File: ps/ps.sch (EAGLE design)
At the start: 66 parts, among them IC1 LM675, Q1 NPN-D, Q2 NPN-D, U1 LM3480IM4, U2 LM317, U3 TLC555CD, U4 LM317, U5 LM317

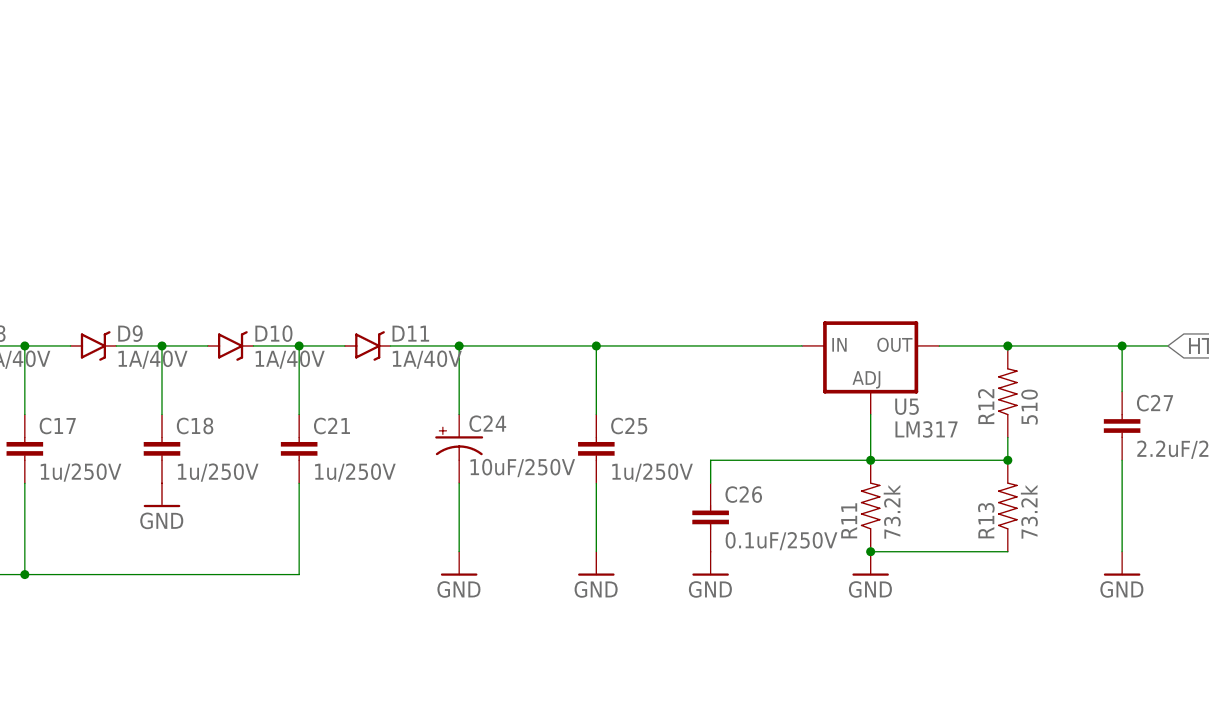
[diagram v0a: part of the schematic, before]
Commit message: Back to 60V supply
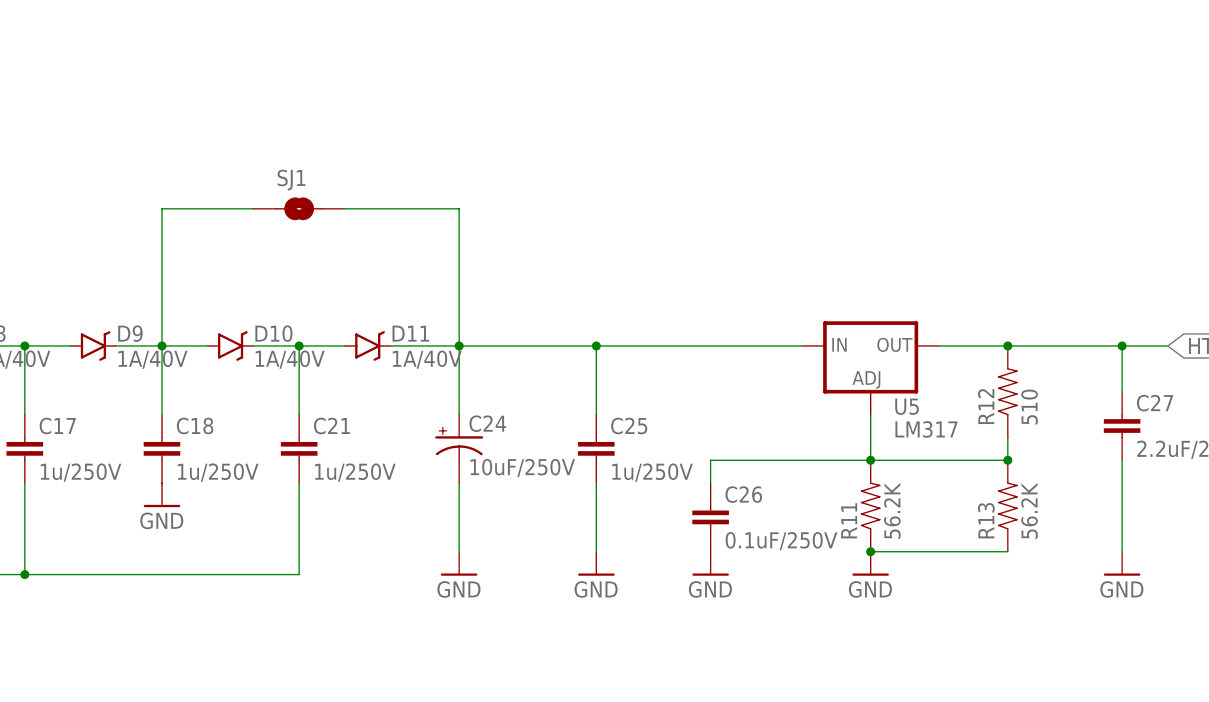
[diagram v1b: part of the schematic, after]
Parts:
- added SJ1: SOLDERJUMPERROUND, my:SOLDERJUMPERROUND
- R11, R13: value 73.2k -> 56.2K
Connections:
- net HV: now also SJ1.2
- net N$15: now also SJ1.1
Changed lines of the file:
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@@
 <part name="C25" library="rcl" deviceset="C-EU" device="C2220K" value="1u/250V"/>
 <part name="GND20" library="SparkFun-Aesthetics" deviceset="GND" device=""/>
-<part name="R11" library="SparkFun-Resistors" deviceset="RESISTOR" device="PTH-1/4W" value="73.2k"/>
-<part name="R13" library="SparkFun-Resistors" deviceset="RESISTOR" device="PTH-1/4W" value="73.2k"/>
+<part name="R11" library="SparkFun-Resistors" deviceset="RESISTOR" device="PTH-1/4W" value="56.2K"/>
+<part name="R13" library="SparkFun-Resistors" deviceset="RESISTOR" device="PTH-1/4W" value="56.2K"/>
 <part name="GND22" library="SparkFun-Aesthetics" deviceset="GND" device=""/>
 <part name="R12" library="SparkFun-Resistors" deviceset="RESISTOR" device="PTH-1/4W" value="510"/>
@@
 <part name="GND24" library="SparkFun-Aesthetics" deviceset="GND" device=""/>
 <part name="R14" library="SparkFun-Resistors" deviceset="100KOHM-1/10W-1%(0603)" device="" value="100k"/>
+<part name="SJ1" library="my" deviceset="SOLDERJUMPER" device="ROUND" value=""/>
 </parts>
 <sheets>
@@
 <instance part="GND24" gate="1" x="109.22" y="200.66" rot="R90"/>
 <instance part="R14" gate="G$1" x="119.38" y="203.2"/>
+<instance part="SJ1" gate="1" x="269.24" y="121.92"/>
 </instances>
 <busses>
@@
 <wire x1="254" y1="99.06" x2="254" y2="106.68" width="0.1524" layer="91"/>
 <junction x="254" y="106.68"/>
+<wire x1="254" y1="106.68" x2="254" y2="121.92" width="0.1524" layer="91"/>
+<pinref part="SJ1" gate="1" pin="1"/>
+<wire x1="254" y1="121.92" x2="264.16" y2="121.92" width="0.1524" layer="91"/>
 </segment>
 </net>
@@
 <wire x1="302.26" y1="99.06" x2="302.26" y2="106.68" width="0.1524" layer="91"/>
 <junction x="302.26" y="106.68"/>
-</segment>
-<segment>
+<pinref part="SJ1" gate="1" pin="2"/>
+<wire x1="274.32" y1="121.92" x2="287.02" y2="121.92" width="0.1524" layer="91"/>
+<wire x1="287.02" y1="121.92" x2="287.02" y2="106.68" width="0.1524" layer="91"/>
+</segment>
+<segment>

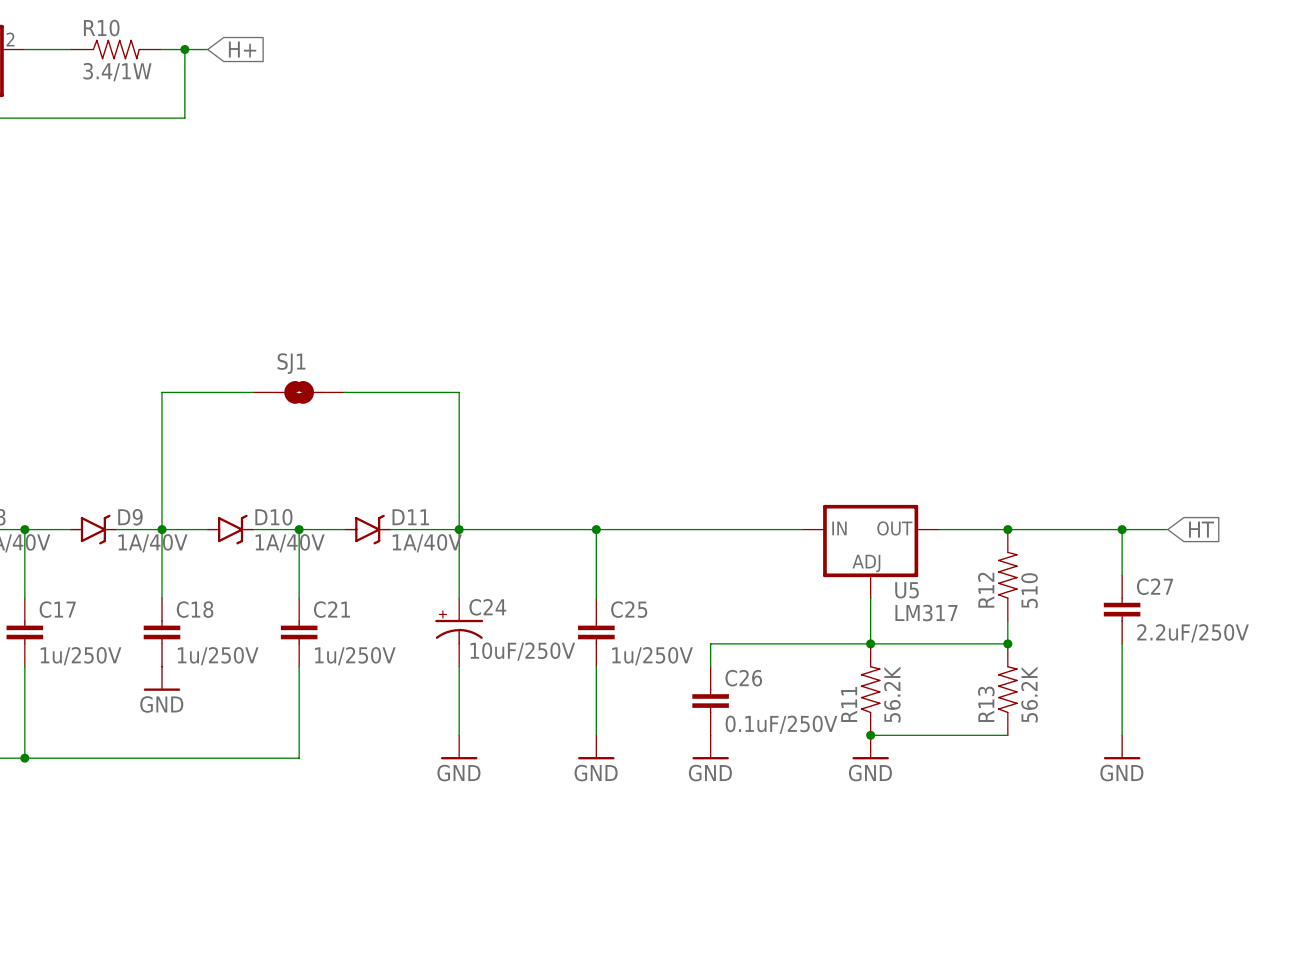
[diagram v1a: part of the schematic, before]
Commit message: HV for neon bulb
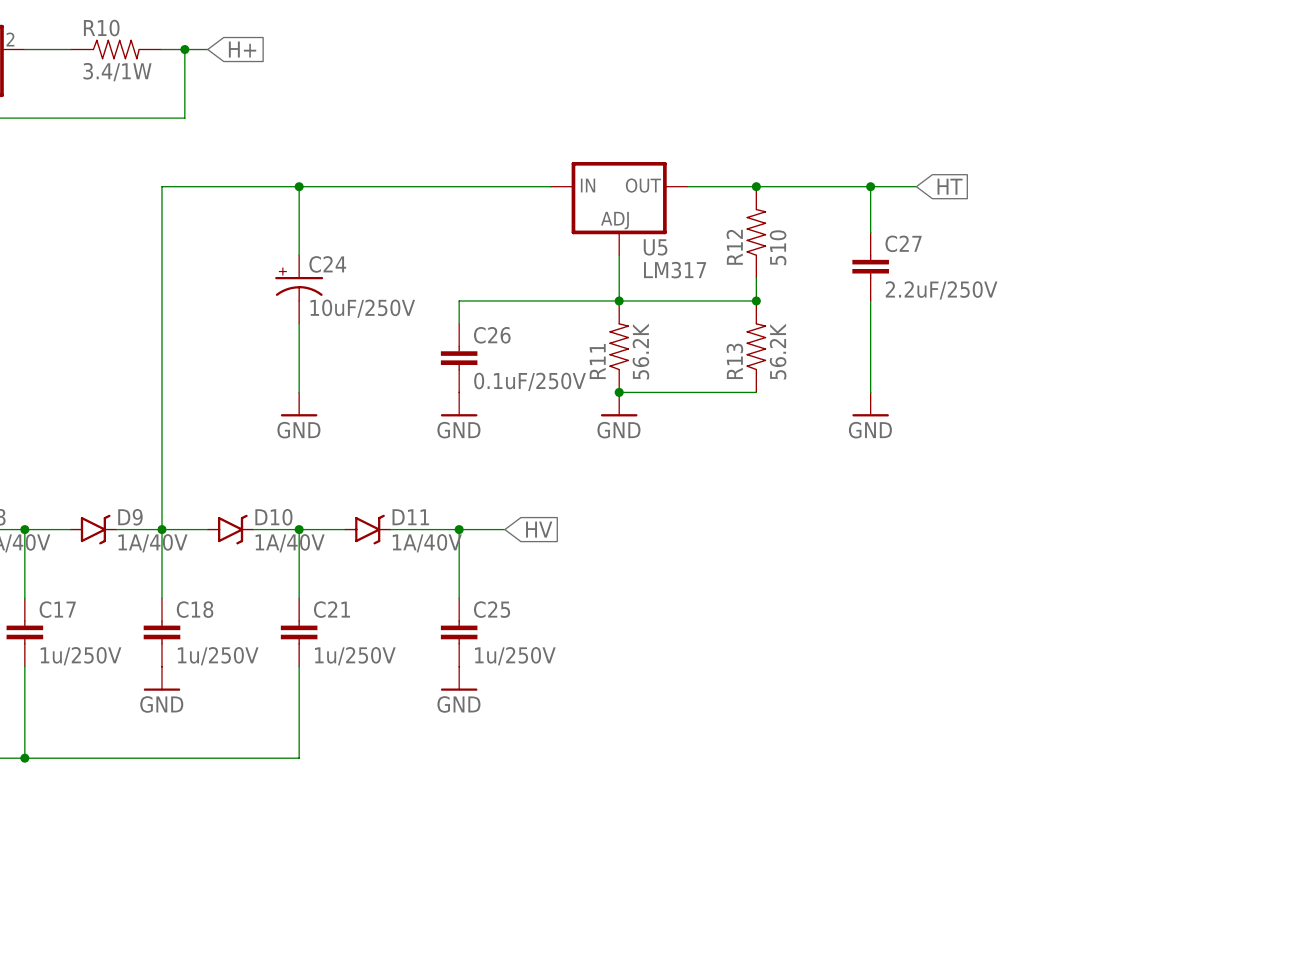
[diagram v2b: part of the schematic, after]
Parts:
- removed SJ1: SOLDERJUMPERROUND, my:SOLDERJUMPERROUND
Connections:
- net HV: no longer C24.+, SJ1.2, U5.IN
- net N$15: now also C24.+, U5.IN; no longer SJ1.1
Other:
- moved on the sheet: C24, C25, C26, C27, R11, R12, R13, U5
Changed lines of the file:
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@@
 <part name="GND24" library="SparkFun-Aesthetics" deviceset="GND" device=""/>
 <part name="R14" library="SparkFun-Resistors" deviceset="100KOHM-1/10W-1%(0603)" device="" value="100k"/>
-<part name="SJ1" library="my" deviceset="SOLDERJUMPER" device="ROUND" value=""/>
 </parts>
 <sheets>
@@
 <instance part="GND14" gate="1" x="223.52" y="88.9"/>
 <instance part="GND16" gate="1" x="254" y="88.9"/>
-<instance part="C24" gate="G$1" x="287.02" y="96.52"/>
-<instance part="GND19" gate="1" x="287.02" y="81.28"/>
-<instance part="U5" gate="G$1" x="332.74" y="106.68"/>
-<instance part="C25" gate="G$1" x="302.26" y="96.52"/>
-<instance part="GND20" gate="1" x="302.26" y="81.28"/>
-<instance part="R11" gate="G$1" x="332.74" y="88.9" rot="R90"/>
-<instance part="R13" gate="G$1" x="347.98" y="88.9" rot="R90"/>
-<instance part="GND22" gate="1" x="332.74" y="81.28"/>
-<instance part="R12" gate="G$1" x="347.98" y="101.6" rot="R90"/>
-<instance part="C26" gate="G$1" x="314.96" y="88.9"/>
-<instance part="GND21" gate="1" x="314.96" y="81.28"/>
-<instance part="C27" gate="G$1" x="360.68" y="99.06"/>
-<instance part="GND23" gate="1" x="360.68" y="81.28"/>
+<instance part="C24" gate="G$1" x="269.24" y="134.62"/>
+<instance part="GND19" gate="1" x="269.24" y="119.38"/>
+<instance part="U5" gate="G$1" x="304.8" y="144.78"/>
+<instance part="C25" gate="G$1" x="287.02" y="96.52"/>
+<instance part="GND20" gate="1" x="287.02" y="88.9"/>
+<instance part="R11" gate="G$1" x="304.8" y="127" rot="R90"/>
+<instance part="R13" gate="G$1" x="320.04" y="127" rot="R90"/>
+<instance part="GND22" gate="1" x="304.8" y="119.38"/>
+<instance part="R12" gate="G$1" x="320.04" y="139.7" rot="R90"/>
+<instance part="C26" gate="G$1" x="287.02" y="127"/>
+<instance part="GND21" gate="1" x="287.02" y="119.38"/>
+<instance part="C27" gate="G$1" x="332.74" y="137.16"/>
+<instance part="GND23" gate="1" x="332.74" y="119.38"/>
 <instance part="IC1" gate="G$1" x="241.3" y="208.28"/>
 <instance part="GND15" gate="1" x="238.76" y="198.12"/>
@@
 <instance part="GND24" gate="1" x="109.22" y="200.66" rot="R90"/>
 <instance part="R14" gate="G$1" x="119.38" y="203.2"/>
-<instance part="SJ1" gate="1" x="269.24" y="121.92"/>
 </instances>
 <busses>
@@
 <pinref part="C24" gate="G$1" pin="-"/>
 <pinref part="GND19" gate="1" pin="GND"/>
-<wire x1="287.02" y1="83.82" x2="287.02" y2="91.44" width="0.1524" layer="91"/>
+<wire x1="269.24" y1="121.92" x2="269.24" y2="129.54" width="0.1524" layer="91"/>
 </segment>
 <segment>
 <pinref part="C25" gate="G$1" pin="2"/>
 <pinref part="GND20" gate="1" pin="GND"/>
-<wire x1="302.26" y1="83.82" x2="302.26" y2="91.44" width="0.1524" layer="91"/>
 </segment>
 <segment>
 <pinref part="R13" gate="G$1" pin="1"/>
 <pinref part="R11" gate="G$1" pin="1"/>
-<wire x1="347.98" y1="83.82" x2="332.74" y2="83.82" width="0.1524" layer="91"/>
+<wire x1="320.04" y1="121.92" x2="304.8" y2="121.92" width="0.1524" layer="91"/>
 <pinref part="GND22" gate="1" pin="GND"/>
-<junction x="332.74" y="83.82"/>
+<junction x="304.8" y="121.92"/>
 </segment>
 <segment>
@@
 <segment>
 <pinref part="C27" gate="G$1" pin="2"/>
-<wire x1="360.68" y1="93.98" x2="360.68" y2="83.82" width="0.1524" layer="91"/>
+<wire x1="332.74" y1="132.08" x2="332.74" y2="121.92" width="0.1524" layer="91"/>
 <pinref part="GND23" gate="1" pin="GND"/>
 </segment>
@@
 <wire x1="254" y1="99.06" x2="254" y2="106.68" width="0.1524" layer="91"/>
 <junction x="254" y="106.68"/>
-<wire x1="254" y1="106.68" x2="254" y2="121.92" width="0.1524" layer="91"/>
-<pinref part="SJ1" gate="1" pin="1"/>
-<wire x1="254" y1="121.92" x2="264.16" y2="121.92" width="0.1524" layer="91"/>
+<wire x1="254" y1="106.68" x2="254" y2="144.78" width="0.1524" layer="91"/>
+<pinref part="U5" gate="G$1" pin="IN"/>
+<wire x1="254" y1="144.78" x2="269.24" y2="144.78" width="0.1524" layer="91"/>
+<pinref part="C24" gate="G$1" pin="+"/>
+<wire x1="269.24" y1="144.78" x2="297.18" y2="144.78" width="0.1524" layer="91"/>
+<wire x1="269.24" y1="137.16" x2="269.24" y2="144.78" width="0.1524" layer="91"/>
+<junction x="269.24" y="144.78"/>
 </segment>
 </net>
@@
 <pinref part="D11" gate="G$1" pin="C"/>
 <wire x1="279.4" y1="106.68" x2="287.02" y2="106.68" width="0.1524" layer="91"/>
-<pinref part="C24" gate="G$1" pin="+"/>
-<wire x1="287.02" y1="106.68" x2="287.02" y2="99.06" width="0.1524" layer="91"/>
+<pinref part="C25" gate="G$1" pin="1"/>
+<wire x1="287.02" y1="99.06" x2="287.02" y2="106.68" width="0.1524" layer="91"/>
+<wire x1="287.02" y1="106.68" x2="292.1" y2="106.68" width="0.1524" layer="91"/>
 <junction x="287.02" y="106.68"/>
-<pinref part="U5" gate="G$1" pin="IN"/>
-<wire x1="287.02" y1="106.68" x2="302.26" y2="106.68" width="0.1524" layer="91"/>
-<pinref part="C25" gate="G$1" pin="1"/>
-<wire x1="302.26" y1="106.68" x2="325.12" y2="106.68" width="0.1524" layer="91"/>
-<wire x1="302.26" y1="99.06" x2="302.26" y2="106.68" width="0.1524" layer="91"/>
-<junction x="302.26" y="106.68"/>
-<pinref part="SJ1" gate="1" pin="2"/>
-<wire x1="274.32" y1="121.92" x2="287.02" y2="121.92" width="0.1524" layer="91"/>
-<wire x1="287.02" y1="121.92" x2="287.02" y2="106.68" width="0.1524" layer="91"/>
+<label x="292.1" y="106.68" size="1.778" layer="95" xref="yes"/>
 </segment>
 <segment>
@@
 <pinref part="U5" gate="G$1" pin="ADJ"/>
 <pinref part="R11" gate="G$1" pin="2"/>
-<wire x1="332.74" y1="99.06" x2="332.74" y2="93.98" width="0.1524" layer="91"/>
+<wire x1="304.8" y1="137.16" x2="304.8" y2="132.08" width="0.1524" layer="91"/>
 <pinref part="R13" gate="G$1" pin="2"/>
-<wire x1="347.98" y1="93.98" x2="332.74" y2="93.98" width="0.1524" layer="91"/>
-<junction x="332.74" y="93.98"/>
+<wire x1="320.04" y1="132.08" x2="304.8" y2="132.08" width="0.1524" layer="91"/>
+<junction x="304.8" y="132.08"/>
 <pinref part="R12" gate="G$1" pin="1"/>
-<junction x="347.98" y="93.98"/>
-<wire x1="347.98" y1="93.98" x2="347.98" y2="96.52" width="0.1524" layer="91"/>
-<wire x1="332.74" y1="93.98" x2="314.96" y2="93.98" width="0.1524" layer="91"/>
+<junction x="320.04" y="132.08"/>
+<wire x1="320.04" y1="132.08" x2="320.04" y2="134.62" width="0.1524" layer="91"/>
+<wire x1="304.8" y1="132.08" x2="287.02" y2="132.08" width="0.1524" layer="91"/>
 <pinref part="C26" gate="G$1" pin="1"/>
-<wire x1="314.96" y1="93.98" x2="314.96" y2="91.44" width="0.1524" layer="91"/>
+<wire x1="287.02" y1="132.08" x2="287.02" y2="129.54" width="0.1524" layer="91"/>
 </segment>
 </net>
@@
 <pinref part="U5" gate="G$1" pin="OUT"/>
 <pinref part="R12" gate="G$1" pin="2"/>
-<wire x1="340.36" y1="106.68" x2="347.98" y2="106.68" width="0.1524" layer="91"/>
-<wire x1="347.98" y1="106.68" x2="360.68" y2="106.68" width="0.1524" layer="91"/>
-<junction x="347.98" y="106.68"/>
+<wire x1="312.42" y1="144.78" x2="320.04" y2="144.78" width="0.1524" layer="91"/>
+<wire x1="320.04" y1="144.78" x2="332.74" y2="144.78" width="0.1524" layer="91"/>
+<junction x="320.04" y="144.78"/>
 <pinref part="C27" gate="G$1" pin="1"/>
-<wire x1="360.68" y1="106.68" x2="360.68" y2="101.6" width="0.1524" layer="91"/>
-<wire x1="360.68" y1="106.68" x2="365.76" y2="106.68" width="0.1524" layer="91"/>
-<junction x="360.68" y="106.68"/>
-<label x="365.76" y="106.68" size="1.778" layer="95" xref="yes"/>
-</segment>
-<segment>
+<wire x1="332.74" y1="144.78" x2="332.74" y2="139.7" width="0.1524" layer="91"/>
+<wire x1="332.74" y1="144.78" x2="337.82" y2="144.78" width="0.1524" layer="91"/>
+<junction x="332.74" y="144.78"/>
+<label x="337.82" y="144.78" size="1.778" layer="95" xref="yes"/>
+</segment>
+<segment>

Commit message: Some tweaks
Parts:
- added R15: 6.8/0.5W, SparkFun-Resistors:RESISTORPTH-1/2W
- R10: value 3.4/1W -> 6.8/0.5W; device SparkFun-Resistors:RESISTORPTH-1W -> SparkFun-Resistors:RESISTORPTH-1/2W
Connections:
- net H+: now also R15.2
- net N$8: now also R15.1
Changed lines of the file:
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@@
 <part name="X3" library="con-wago-508" deviceset="W237-05P" device=""/>
 <part name="GND9" library="SparkFun-Aesthetics" deviceset="GND" device=""/>
-<part name="R10" library="SparkFun-Resistors" deviceset="RESISTOR" device="PTH-1W" value="3.4/1W"/>
+<part name="R10" library="SparkFun-Resistors" deviceset="RESISTOR" device="PTH-1/2W" value="6.8/0.5W"/>
 <part name="U4" library="my" deviceset="LM317" device=""/>
 <part name="J1" library="SparkFun-Connectors" deviceset="M02" device="PTH"/>
 <part name="GND24" library="SparkFun-Aesthetics" deviceset="GND" device=""/>
 <part name="R14" library="SparkFun-Resistors" deviceset="100KOHM-1/10W-1%(0603)" device="" value="100k"/>
+<part name="R15" library="SparkFun-Resistors" deviceset="RESISTOR" device="PTH-1/2W" value="6.8/0.5W"/>
 </parts>
 <sheets>
@@
 <instance part="GND24" gate="1" x="109.22" y="200.66" rot="R90"/>
 <instance part="R14" gate="G$1" x="119.38" y="203.2"/>
+<instance part="R15" gate="G$1" x="248.92" y="170.18"/>
 </instances>
 <busses>
@@
 <junction x="256.54" y="160.02"/>
 <label x="259.08" y="160.02" size="1.778" layer="95" xref="yes"/>
+<wire x1="256.54" y1="160.02" x2="256.54" y2="170.18" width="0.1524" layer="91"/>
+<pinref part="R15" gate="G$1" pin="2"/>
+<wire x1="256.54" y1="170.18" x2="254" y2="170.18" width="0.1524" layer="91"/>
 </segment>
 </net>
@@
 <pinref part="U4" gate="U1" pin="VO"/>
 <pinref part="R10" gate="G$1" pin="1"/>
-<wire x1="238.76" y1="160.02" x2="243.84" y2="160.02" width="0.1524" layer="91"/>
-</segment>
-</net>
+<wire x1="238.76" y1="160.02" x2="241.3" y2="160.02" width="0.1524" layer="91"/>
+<wire x1="241.3" y1="160.02" x2="243.84" y2="160.02" width="0.1524" layer="91"/>
+<wire x1="241.3" y1="160.02" x2="241.3" y2="170.18" width="0.1524" layer="91"/>
+<junction x="241.3" y="160.02"/>
+<pinref part="R15" gate="G$1" pin="1"/>
+<wire x1="241.3" y1="170.18" x2="243.84" y2="170.18" width="0.1524" layer="91"/>
+</segment>
+</net>

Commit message: PSU tweaked
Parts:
- R5: value 4.7K -> 1K/0.5W; device SparkFun-Resistors:4.7KOHM-1/10W-1%(0603) -> rcl:R-US_R1210W
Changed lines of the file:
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@@
 <part name="C9" library="SparkFun-Capacitors" deviceset="4.7NF-50V-10%(0603)" device="" value="0.47nF"/>
 <part name="GND10" library="SparkFun-Aesthetics" deviceset="GND" device=""/>
-<part name="R5" library="SparkFun-Resistors" deviceset="4.7KOHM-1/10W-1%(0603)" device="" value="4.7K"/>
+<part name="R5" library="rcl" deviceset="R-US_" device="R1210W" value="1K/0.5W"/>
 <part name="D3" library="SparkFun-DiscreteSemi" deviceset="DIODE-SCHOTTKY" device="-B340A" value="1A/40V"/>
 <part name="D4" library="SparkFun-DiscreteSemi" deviceset="DIODE-SCHOTTKY" device="-B340A" value="1A/40V"/>
